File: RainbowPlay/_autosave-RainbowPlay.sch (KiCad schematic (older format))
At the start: 47 parts, among them J1 GPIO_CONNECTOR, J2 PJ-102A, U1 LM386, U2 LM386

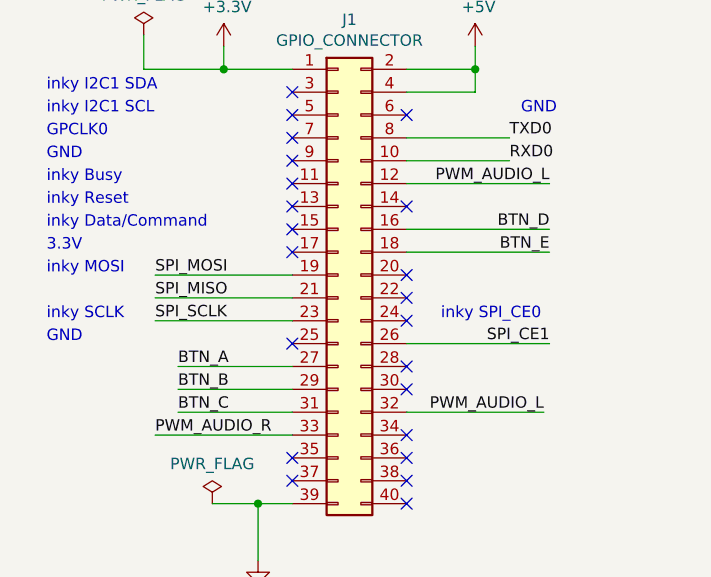
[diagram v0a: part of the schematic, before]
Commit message: General dev on PCB
Ensure GPIO pinouts are correct
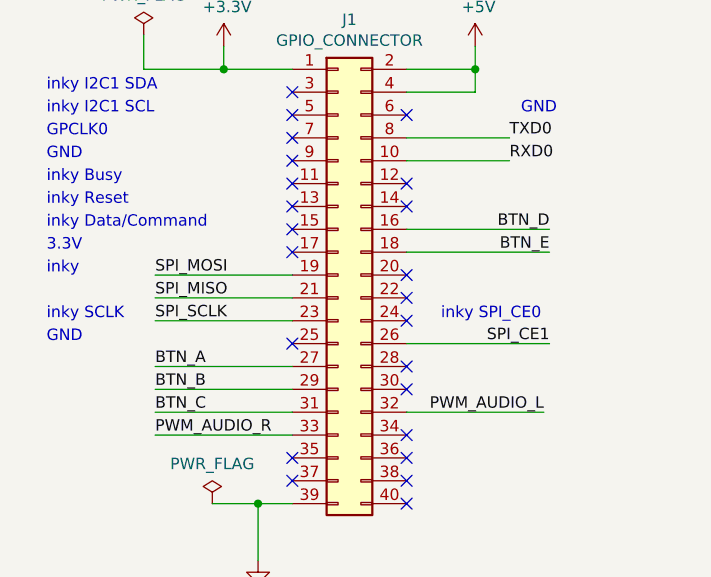
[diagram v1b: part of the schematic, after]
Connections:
- wire segments 166 -> 165
- no-connect marks 69 -> 70
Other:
- note added: "inky"
- note removed: "inky MOSI"
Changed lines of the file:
@@
 Text Label 3350 2275 0    50   ~ 0
 RXD0
-Text Label 3525 2375 2    50   ~ 0
-PWM_AUDIO_L
 Text Label 3525 3075 2    50   ~ 0
 SPI_CE1
@@
 Factory reset
 NoConn ~ 7350 5550
-Wire Wire Line
-	2900 2375 3525 2375
 NoConn ~ 2900 3775
 NoConn ~ 2900 3675
@@
 	14700 8425 14700 8625
 NoConn ~ 2400 2375
-Text Label 1900 3175 0    50   ~ 0
+Text Label 1800 3175 0    50   ~ 0
 BTN_A
-Text Label 1900 3275 0    50   ~ 0
+Text Label 1800 3275 0    50   ~ 0
 BTN_B
-Text Label 1900 3375 0    50   ~ 0
+Text Label 1800 3375 0    50   ~ 0
 BTN_C
 Text Label 3525 2575 2    50   ~ 0
@@
 Text Notes 1325 2975 0    50   ~ 0
 inky SCLK
-Text Notes 1325 2775 0    50   ~ 0
-inky MOSI
-Text Notes 1325 2375 0    50   ~ 0
-inky Busy
-Text Notes 1325 2475 0    50   ~ 0
-inky Reset
-Text Notes 1325 2575 0    50   ~ 0
-inky Data/Command
-Wire Wire Line
-	2400 3375 1900 3375
-Wire Wire Line
-	1900 3275 2400 3275
-Wire Wire Line
-	2400 3175 1900 3175
+Wire Wire Line
+	2400 3375 1800 3375
+Wire Wire Line
+	1800 3275 2400 3275
+Wire Wire Line
+	2400 3175 1800 3175
 NoConn ~ 2400 2475
 NoConn ~ 2400 2575
-Text Notes 1325 2275 0    50   ~ 0
-GND
-Text Notes 1325 2675 0    50   ~ 0
-3.3V
 NoConn ~ 2400 2675
 NoConn ~ 2400 1975
 NoConn ~ 2400 2075
-Text Notes 1325 2175 0    50   ~ 0
-GPCLK0
 NoConn ~ 2400 2175
-Text Notes 1325 2075 0    50   ~ 0
-inky I2C1 SCL
-Text Notes 1325 1975 0    50   ~ 0
-inky I2C1 SDA
 Text Notes 1325 3075 0    50   ~ 0
 GND
 Text Notes 3400 2075 0    50   ~ 0
 GND
+NoConn ~ 2900 2375
+Text Notes 1325 2775 0    50   ~ 0
+inky
+Text Notes 1325 2675 0    50   ~ 0
+3.3V
+Text Notes 1325 1975 0    50   ~ 0
+inky I2C1 SDA
+Text Notes 1325 2075 0    50   ~ 0
+inky I2C1 SCL
+Text Notes 1325 2175 0    50   ~ 0
+GPCLK0
+Text Notes 1325 2275 0    50   ~ 0
+GND
+Text Notes 1325 2575 0    50   ~ 0
+inky Data/Command
+Text Notes 1325 2475 0    50   ~ 0
+inky Reset
+Text Notes 1325 2375 0    50   ~ 0
+inky Busy
 $EndSCHEMATC
